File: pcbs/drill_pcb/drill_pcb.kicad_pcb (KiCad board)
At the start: 2 copper layers, 240 x 100 mm, 78 parts, among them J201 THERMOMETER, J301 TOP BOARD, J302 STEPPER 1, J306 STEPPER 2, J307 TOF SENSOR, J401 ROTARY ENCODER, J402 STRAIN GAUGE, J403 STORAGE STEPPER, SW101 RPi reset, U101 TXS0108EPW, U102 Pico, U201 IFX007T, U202 IFX007T, U203 ACS712xLCTR-20A, U401 HT75xx-1-SOT89

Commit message: PCB update
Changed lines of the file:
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@@
 			(at 4 5.2 0)
 			(layer "F.SilkS")
-			(hide yes)
 			(effects
 				(font
@@
 		(tags "capacitor handsolder")
 		(property "Reference" "C102"
-			(at 0 2 360)
+			(at 0 2 0)
 			(layer "F.SilkS")
 			(effects
@@
 		)
 		(property "Value" "100n"
-			(at 0.0375 4 360)
+			(at 0.0375 4 0)
 			(layer "F.Fab")
 			(effects
@@
 		)
 		(fp_text user "${REFERENCE}"
-			(at 0 0 360)
+			(at 0 0 0)
 			(layer "F.Fab")
 			(effects
@@
 		(tags "capacitor handsolder")
 		(property "Reference" "C101"
-			(at 0 1.85 360)
+			(at 0 1.85 0)
 			(layer "B.SilkS")
 			(effects
@@
 		)
 		(property "Value" "100n"
-			(at 0 -1.85 360)
+			(at 0 -1.85 0)
 			(layer "B.Fab")
 			(effects
@@
 		)
 		(fp_text user "${REFERENCE}"
-			(at 0 0 360)
+			(at 0 0 0)
 			(layer "B.Fab")
 			(effects

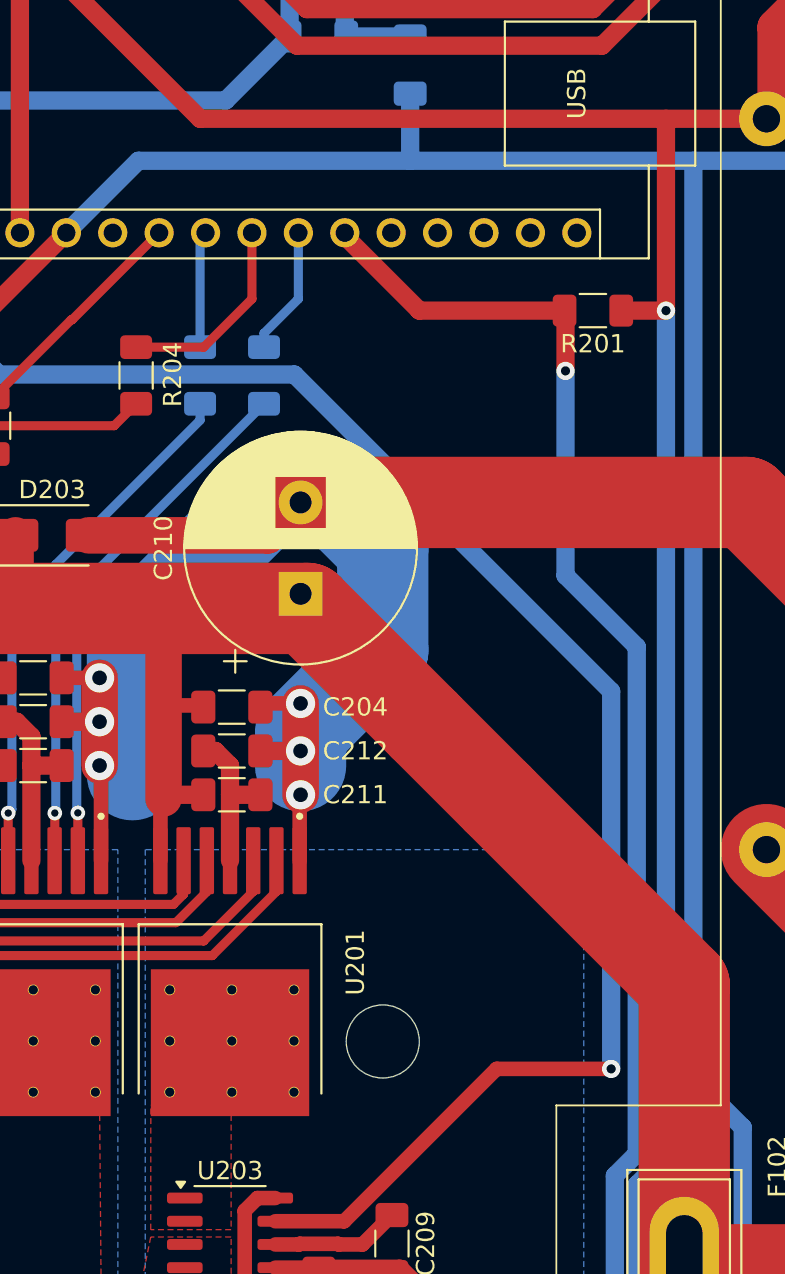
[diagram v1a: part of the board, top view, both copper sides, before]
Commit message: H-bridge IN pins connected to fast PWM Arduino pins on both schematic and PCB.
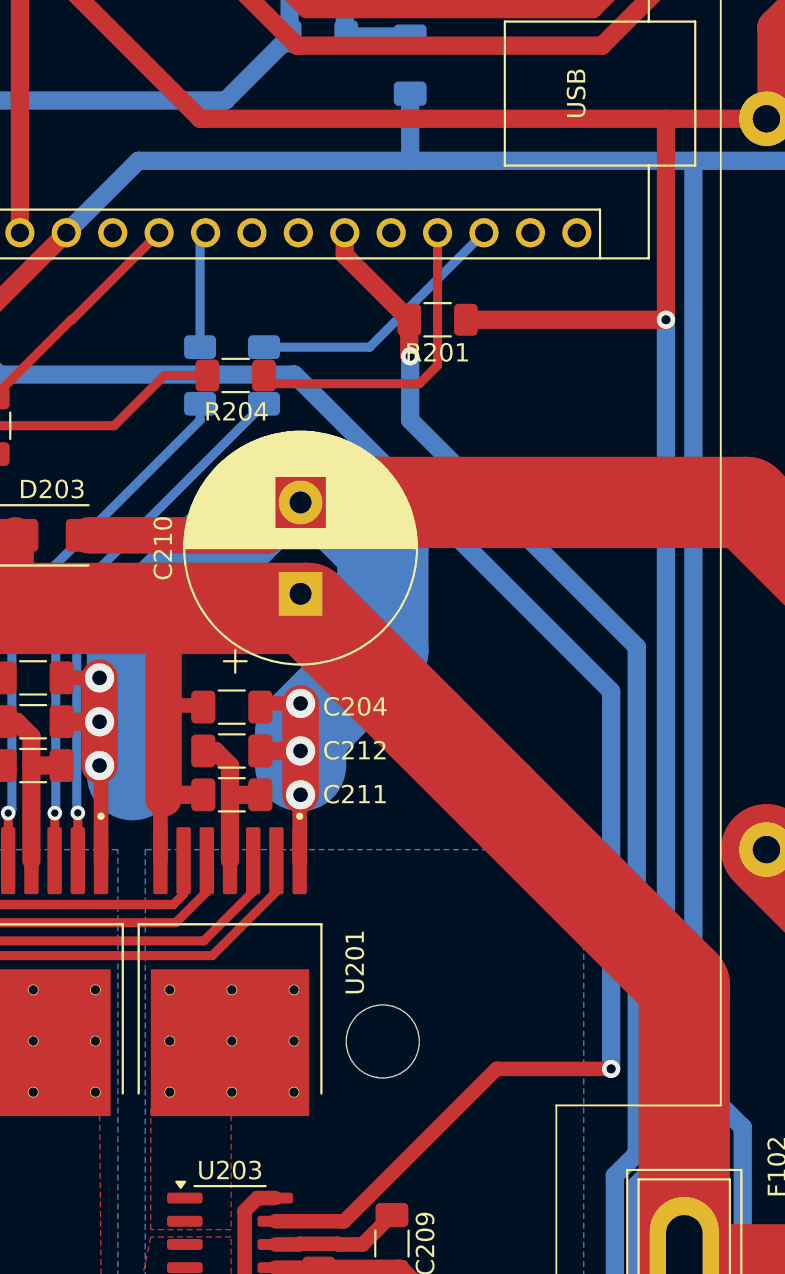
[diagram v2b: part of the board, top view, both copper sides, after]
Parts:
- C401, C402: value C_Polarized -> 10u
- moved R201 8.51 mm to (138.5, 125.0)
- moved R204 5.45 mm to (127.5, 128.1), turned to 0 degrees
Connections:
- A201 pad 12: unconnected-(A201-D9-Pad12) -> Net-(A201-D9)
- A201 pad 13: unconnected-(A201-D10-Pad13) -> Net-(A201-D10)
- A201 pad 8: Net-(A201-D5) -> unconnected-(A201-D5-Pad8)
- A201 pad 9: Net-(A201-D6) -> unconnected-(A201-D6-Pad9)
- R204 pad 2: Net-(A201-D5) -> Net-(A201-D9)
- R206 pad 2: Net-(A201-D6) -> Net-(A201-D10)
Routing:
- net Net-(A201-D9): track 0.00 -> 17.4 mm
- net Net-(A201-D10): track 0.00 -> 14.6 mm
- net Net-(A201-D5): track 11.1 -> 0.00 mm
- net +5V: track 627.9 -> 636.4 mm
- net Net-(A201-D6): track 7.04 -> 0.00 mm
- net Net-(A201-D7): track 102.3 -> 97.6 mm
- net Net-(U201-IN): track 70.9 -> 75.5 mm

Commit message: pcb cleanup
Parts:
- removed 1111401: ~, drill_hx711footp:HX711
- removed A201, A301, A401: Arduino_Nano_v3.x, Module:Arduino_Nano
- removed A302, A303: Driver_TMC2209, Module:Pololu_Breakout-16_15.2x20.3mm
- removed A402: Pololu_Breakout_A4988, Module:Pololu_Breakout-16_15.2x20.3mm
- removed C102, C103, C201, C202, C203, C207: 100n, Capacitor_SMD:C_1206_3216Metric_Pad1.33x1.80mm_HandSolder
- removed C204, C205, C211, C212, C213, C214: 100n/50V, Capacitor_SMD:C_1206_3216Metric_Pad1.33x1.80mm_HandSolder
- removed C206, C208, C209: 1n, Capacitor_SMD:C_1206_3216Metric_Pad1.33x1.80mm_HandSolder
- removed C210: 1000uF/50V, Capacitor_THT:CP_Radial_D12.5mm_P5.00mm
- removed C301, C302: 100μ, Capacitor_THT:CP_Radial_D8.0mm_P3.50mm
- removed C401, C402: 10u, Capacitor_THT:CP_Radial_D5.0mm_P2.50mm
- removed D201, D202: SMAJ5.0CA, Diode_SMD:D_SMA
- removed D203: SMAJ24A, Diode_SMD:D_SMA
- removed Dean201: DRILL MOTOR, drill_T-DEAN:DEANS
- removed G***: LOGO, logo:logo
- removed HEATSINK: drill_heatsink, heatsink:drill_heatsink
- removed J201: THERMOMETER, Connector_JST:JST_XH_B3B-XH-A_1x03_P2.50mm_Vertical
- removed J301: TOP BOARD, Connector_JST:JST_XH_B6B-XH-A_1x06_P2.50mm_Vertical
- removed J302: STEPPER 1, Connector_JST:JST_XH_B4B-XH-A_1x04_P2.50mm_Vertical
- removed J306: STEPPER 2, Connector_JST:JST_XH_B4B-XH-A_1x04_P2.50mm_Vertical
- removed J307: TOF SENSOR, Connector_JST:JST_XH_B3B-XH-A_1x03_P2.50mm_Vertical
- removed J401: ROTARY ENCODER, Connector_JST:JST_XH_B4B-XH-A_1x04_P2.50mm_Vertical
- removed J402: STRAIN GAUGE, Connector_JST:JST_XH_B6B-XH-A_1x06_P2.50mm_Vertical
- removed J403: STORAGE STEPPER, Connector_JST:JST_XH_B4B-XH-A_1x04_P2.50mm_Vertical
- removed R101, R202, R203, R204, R205, R206, R207: 10k, Resistor_SMD:R_1206_3216Metric_Pad1.30x1.75mm_HandSolder
- removed R201: 4k7, Resistor_SMD:R_1206_3216Metric_Pad1.30x1.75mm_HandSolder
- removed R208, R209: 820, Resistor_SMD:R_1206_3216Metric_Pad1.30x1.75mm_HandSolder
- removed R210: 330k, Resistor_SMD:R_1206_3216Metric_Pad1.30x1.75mm_HandSolder
- removed R301: 1k, Resistor_SMD:R_1206_3216Metric
- removed REF** (x4): MountingHole_3.2mm_M3, MountingHole:MountingHole_3.2mm_M3
- removed TP401, TP402, TP403, TP404, TP405: TestPoint, TestPoint:TestPoint_Pad_1.5x1.5mm
- removed TP409, TP410, TP411: TestPoint_2Pole, Capacitor_SMD:C_0504_1310Metric_Pad0.83x1.28mm_HandSolder
- removed U101: TXS0108EPW, Package_SO:TSSOP-20_4.4x6.5mm_P0.65mm
- removed U201, U202: IFX007T, drill_IFX007T:TO127P1500X440-8N_plusVias
- removed U203: ACS712xLCTR-20A, Package_SO:SOIC-8_3.9x4.9mm_P1.27mm
- removed U401: HT75xx-1-SOT89, Package_TO_SOT_THT:TO-92L_Inline
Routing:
- net GND: track 1018.7 -> 149.8 mm, vias 8 -> 0
- net +5V: track 636.4 -> 90.7 mm, vias 1 -> 0
- net +24V: track 354.7 -> 40.4 mm
- net /Linear drive control/SDA: track 238.5 -> 0.00 mm, vias 1 -> 0
- net /Linear drive control/SCL: track 236.0 -> 0.00 mm
- net /Motor control/RESET: track 153.1 -> 0.00 mm, vias 1 -> 0
- net Net-(A301-A1): track 137.5 -> 0.00 mm
- net Net-(A301-D11): track 133.3 -> 0.00 mm
- net Net-(A201-A3): track 126.2 -> 0.00 mm, vias 1 -> 0
- net Net-(A301-D9): track 124.7 -> 0.00 mm
- net Net-(A201-A0): track 115.4 -> 0.00 mm, vias 2 -> 0
- net Net-(A301-A0): track 114.6 -> 0.00 mm
- net Net-(A301-D5): track 113.9 -> 0.00 mm
- net Net-(A301-D6): track 100.8 -> 0.00 mm
- net Net-(A201-D7): track 97.6 -> 0.00 mm, vias 1 -> 0
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- removed copper zone on B.Cu, net (none)
- removed copper zone on F.Cu, net (none)
- removed copper zone on F.Cu, net Net-(Dean201-Pin_1)
- removed copper zone on B.Cu, net Net-(Dean201-Pin_2)
- removed copper zone on F.Cu, net Net-(Dean201-Pin_2)
- removed copper zone on B.Cu, net Net-(U201-OUT-Pad8)
- removed copper zone on F.Cu, net Net-(U201-OUT-Pad8)
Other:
- board outline removed
- board text removed: "Brno Drilling Space Mission v1.0.0"

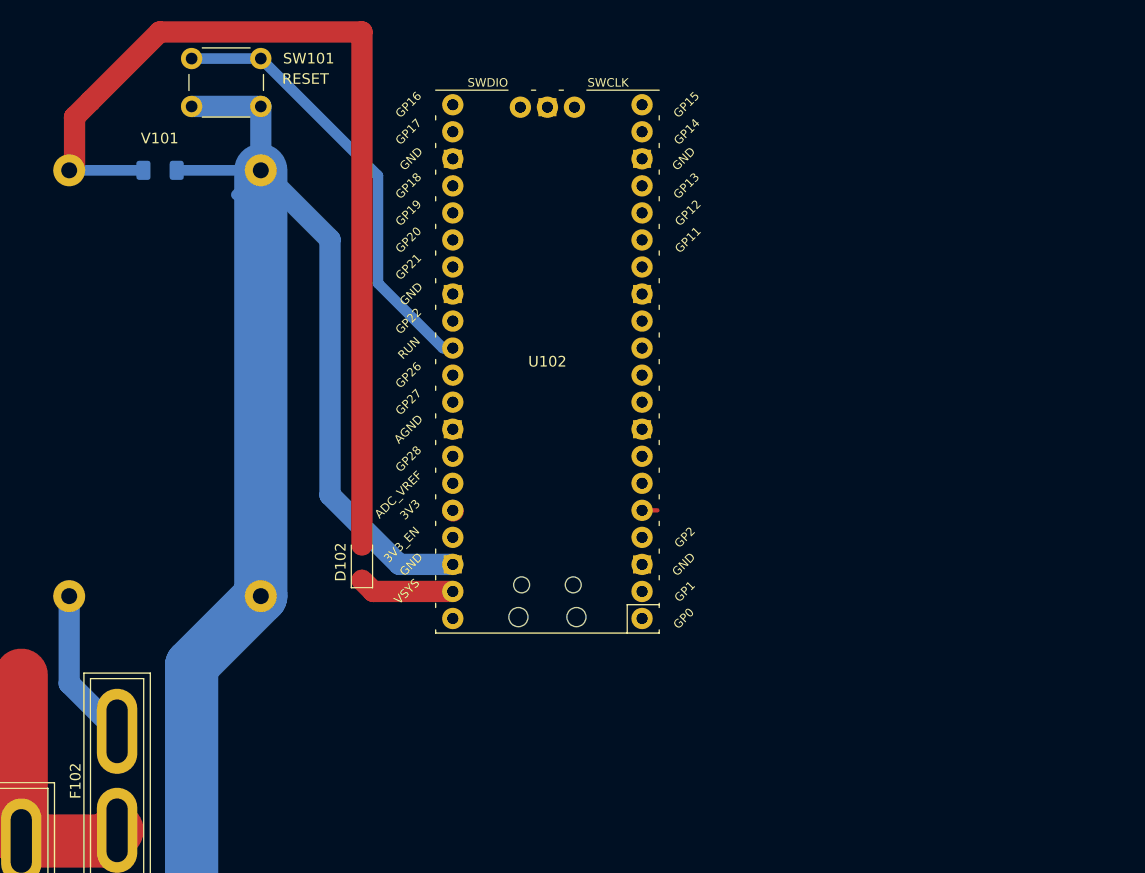
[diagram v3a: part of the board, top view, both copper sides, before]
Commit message: pcb changes, added ESP library
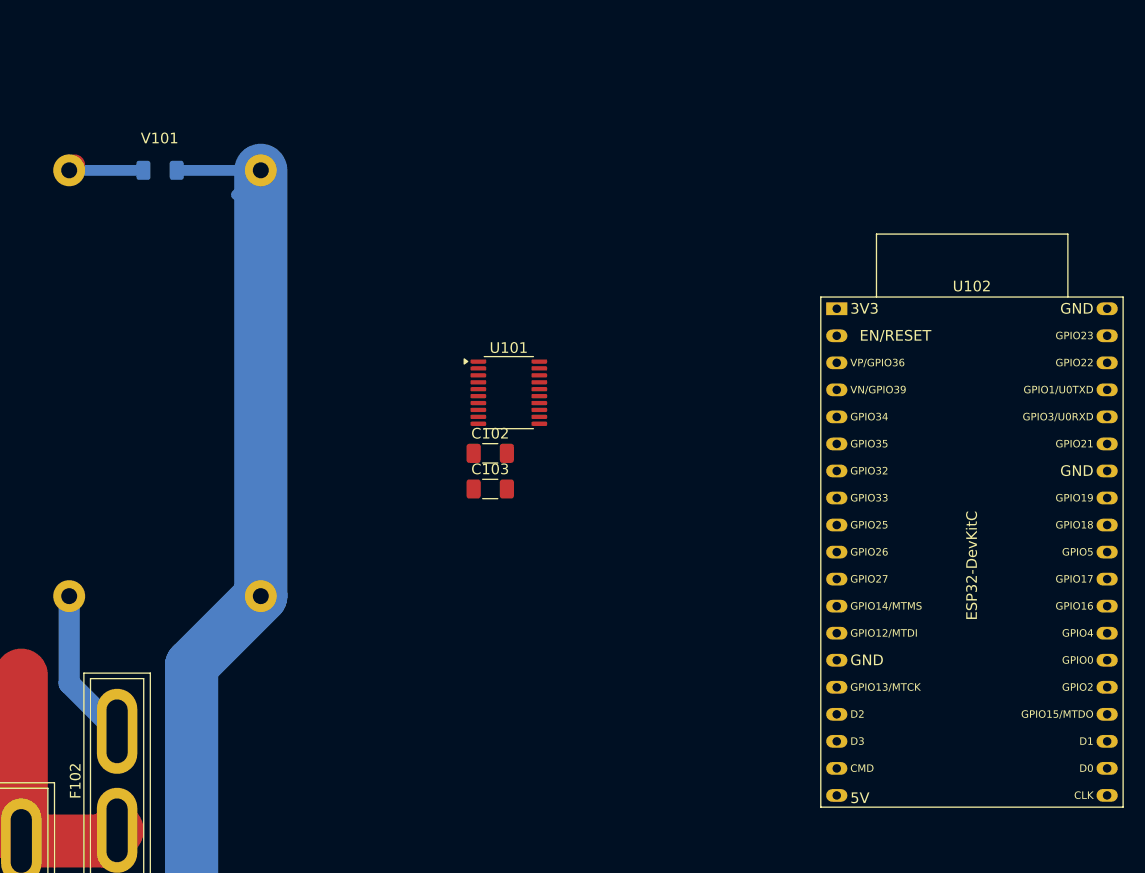
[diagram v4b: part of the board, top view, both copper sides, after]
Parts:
- removed D102: D_Schottky, Diode_SMD:D_SOD-123
- removed SW101: RPi reset, Button_Switch_THT:SW_PUSH_6mm_H5mm
- added C102: 100n, Capacitor_SMD:C_1206_3216Metric_Pad1.33x1.80mm_HandSolder, F.Cu at (196.1, 140.6)
- added C103: 100n, Capacitor_SMD:C_1206_3216Metric_Pad1.33x1.80mm_HandSolder, F.Cu at (196.1, 143.9)
- added U101: TXS0108EPW, Package_SO:TSSOP-20_4.4x6.5mm_P0.65mm, F.Cu at (197.8, 134.9)
- U102: value Pico -> ESP32-DevKitC; footprint drill_RP-Pico Libraries:RPi_Pico_SMD_TH -> PCM_Espressif:ESP32-DevKitC
- moved U102 27.6 mm to (228.6, 127.0), turned to 0 degrees
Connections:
- U102 pad 10: Net-(U101-A4) -> unconnected-(U102-DAC_2/ADC2_CH9/GPIO26-Pad10)
- U102 pad 11: Net-(U101-A3) -> unconnected-(U102-ADC2_CH7/GPIO27-Pad11)
- U102 pad 12: Net-(U101-A2) -> unconnected-(U102-MTMS/GPIO14/ADC2_CH6-Pad12)
- U102 pad 14: unconnected-(U102-GPIO10-Pad14)_1 -> Net-(U102-GND-Pad14)
- U102 pad 30: Net-(U102-RUN) -> unconnected-(U102-GPIO18-Pad30)
- U102 pad 32: unconnected-(U102-GPIO27_ADC1-Pad32)_1 -> Net-(U102-GND-Pad14)
- U102 pad 36: +3.3V -> unconnected-(U102-GPIO22-Pad36)
- U102 pad 38: GND -> Net-(U102-GND-Pad14)
- U102 pad 5: Net-(U101-OE) -> unconnected-(U102-VDET_1/GPIO34/ADC1_CH6-Pad5)
- U102 pad 6: Net-(U101-A8) -> unconnected-(U102-VDET_2/GPIO35/ADC1_CH7-Pad6)
- U102 pad 7: Net-(U101-A7) -> unconnected-(U102-32K_XP/GPIO32/ADC1_CH4-Pad7)
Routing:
- net +5V: track 90.7 -> 7.68 mm
- net GND: track 149.8 -> 89.6 mm
- net Net-(U102-RUN): track 41.7 -> 0.00 mm
- net Net-(D102-K): track 8.97 -> 0.00 mm
- net Net-(U101-OE): track 1.44 -> 0.00 mm
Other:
- board text removed: "RESET"

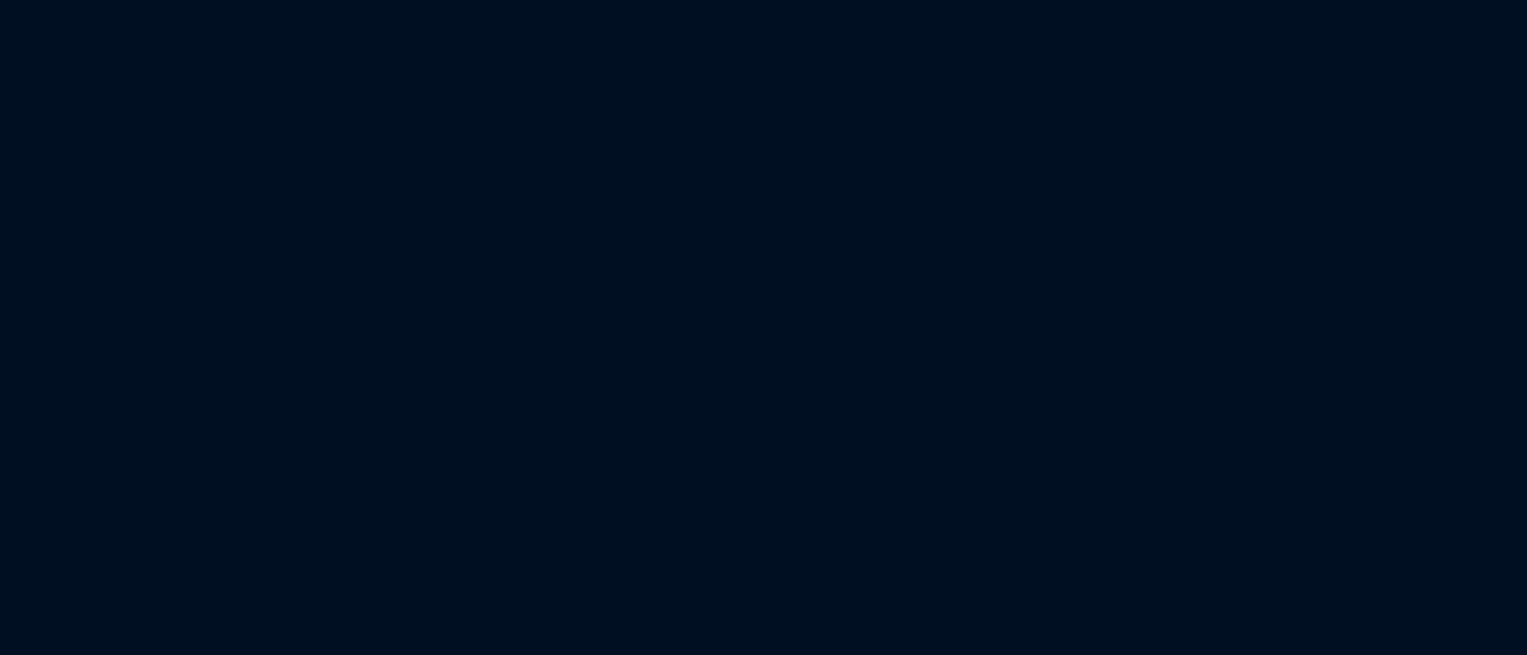
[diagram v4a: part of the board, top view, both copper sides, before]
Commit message: pridany drivery a ldo (nehotove)
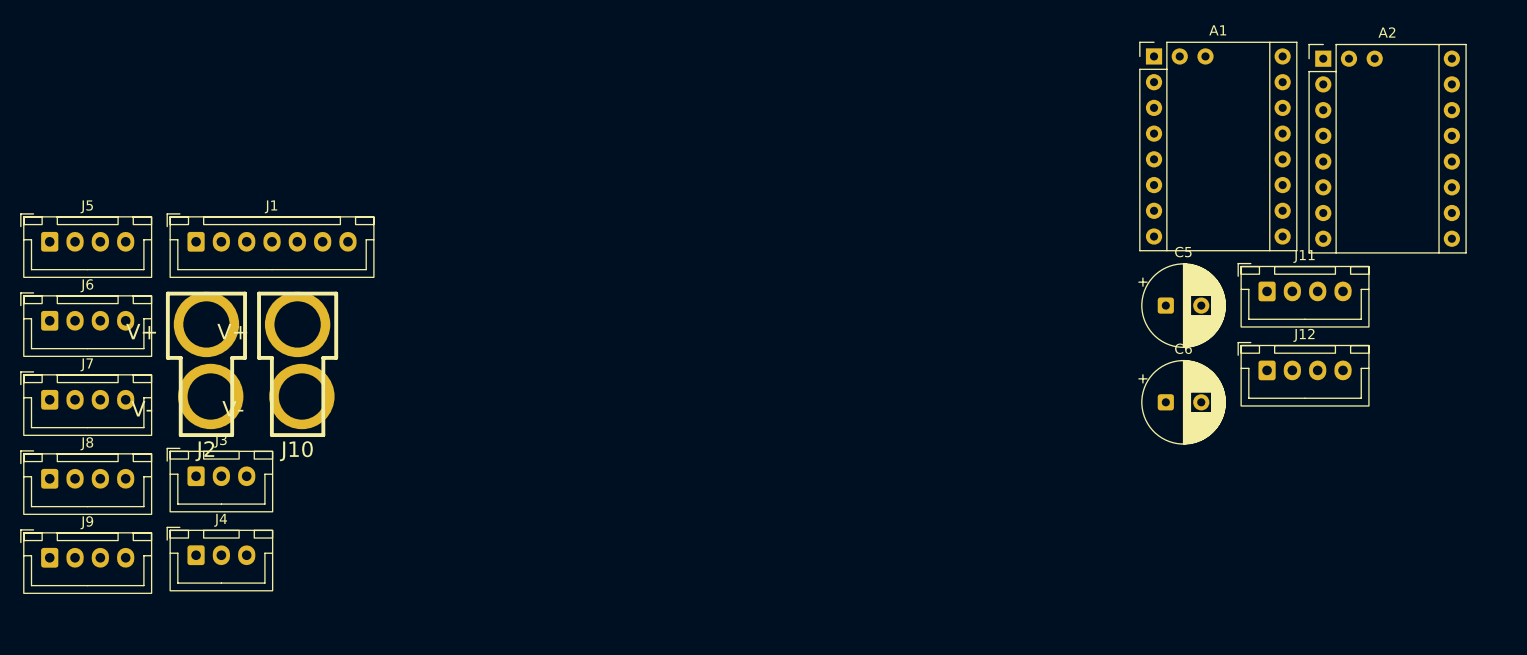
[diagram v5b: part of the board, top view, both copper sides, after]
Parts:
- added A1: Driver_TMC2209, Module:Pololu_Breakout-16_15.2x20.3mm, F.Cu at (207.1, 50.5)
- added A2: Driver_TMC5160, Module:Pololu_Breakout-16_15.2x20.3mm, F.Cu at (223.8, 50.7)
- added C5: 100μ, Capacitor_THT:CP_Radial_D8.0mm_P3.50mm, F.Cu at (208.3, 75.1)
- added C6: 100μ, Capacitor_THT:CP_Radial_D8.0mm_P3.50mm, F.Cu at (208.3, 84.7)
- added J1: WEIGHT SENSOR, Connector_JST:JST_XH_B7B-XH-A_1x07_P2.50mm_Vertical, F.Cu at (112.5, 68.8)
- added J10: DC MOTOR UART, drill_T-DEAN:DEANS, F.Cu at (122.5, 81.5)
- added J11: motor1, Connector_JST:JST_XH_B4B-XH-A_1x04_P2.50mm_Vertical, F.Cu at (218.2, 73.7)
- added J12: motor2, Connector_JST:JST_XH_B4B-XH-A_1x04_P2.50mm_Vertical, F.Cu at (218.2, 81.5)
- added J2: DC MOTOR 24 V, drill_T-DEAN:DEANS, F.Cu at (113.5, 81.5)
- added J3: LIMIT SENSOR TOP, Connector_JST:JST_XH_B3B-XH-A_1x03_P2.50mm_Vertical, F.Cu at (112.5, 92.0)
- added J4: LIMIT SENSOR BOTTOM, Connector_JST:JST_XH_B3B-XH-A_1x03_P2.50mm_Vertical, F.Cu at (112.5, 99.8)
- added J5: ENCODER VERTICAL DRIVE, Connector_JST:JST_XH_B4B-XH-A_1x04_P2.50mm_Vertical, F.Cu at (98.0, 68.8)
- added J6: ENCODER STORAGE, Connector_JST:JST_XH_B4B-XH-A_1x04_P2.50mm_Vertical, F.Cu at (98.0, 76.6)
- added J7: HEIGHT SENSOR, Connector_JST:JST_XH_B4B-XH-A_1x04_P2.50mm_Vertical, F.Cu at (98.0, 84.4)
- added J8: STEPPER VERTICAL DRIVE, Connector_JST:JST_XH_B4B-XH-A_1x04_P2.50mm_Vertical, F.Cu at (98.0, 92.2)
- added J9: STEPPER STORAGE, Connector_JST:JST_XH_B4B-XH-A_1x04_P2.50mm_Vertical, F.Cu at (98.0, 100.0)
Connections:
- U102 pad 14: Net-(U102-GND-Pad14) -> GND
- U102 pad 32: Net-(U102-GND-Pad14) -> GND
- U102 pad 38: Net-(U102-GND-Pad14) -> GND
